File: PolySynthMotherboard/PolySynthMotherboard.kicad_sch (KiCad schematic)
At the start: 0 parts

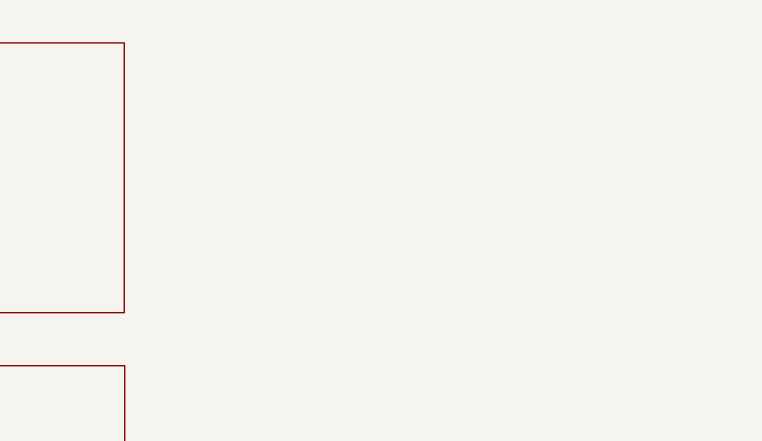
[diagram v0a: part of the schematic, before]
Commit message: op-amp layout improved
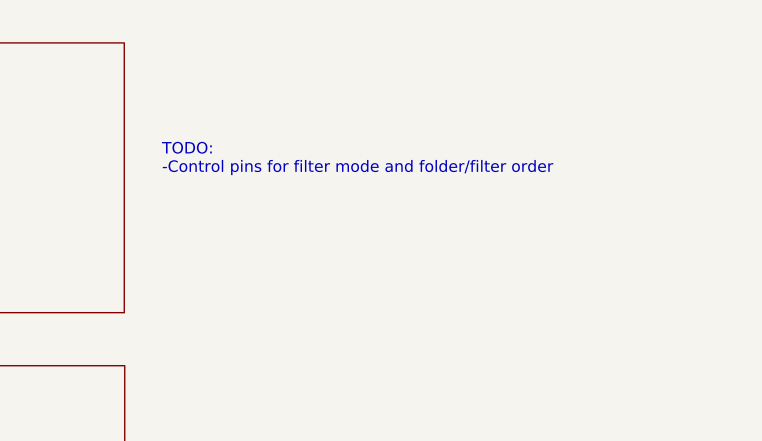
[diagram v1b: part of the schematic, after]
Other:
- note added: "TODO: -Control pins for filter mode and folder/filter order"
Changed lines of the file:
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@@
 (kicad_sch (version 20230121) (generator eeschema)
   (paper "A4")
+  (text "TODO:\n-Control pins for filter mode and folder/filter order"
+    (at 140.081 32.004 0)
+    (effects (font (size 1.27 1.27)) (justify left bottom))
+  )
   (sheet (at 97.7392 53.1368) (size 38.2016 27.7368) (fields_autoplaced)
     (stroke (width 0.1524) (type solid))

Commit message: power supply tweaks
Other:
- note removed: "TODO: -Control pins for filter mode and folder/filter order"
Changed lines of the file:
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@@
 (kicad_sch (version 20230121) (generator eeschema)
   (paper "A4")
-  (text "TODO:\n-Control pins for filter mode and folder/filter order"
-    (at 140.081 32.004 0)
-    (effects (font (size 1.27 1.27)) (justify left bottom))
-  )
   (sheet (at 97.7392 53.1368) (size 38.2016 27.7368) (fields_autoplaced)
     (stroke (width 0.1524) (type solid))
